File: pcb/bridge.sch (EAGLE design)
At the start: 46 parts, among them IC1 MEGA8-AI, IC4 78L05SMD, IC5 LM358D, Q1 16MHz, X1 PN61729-S

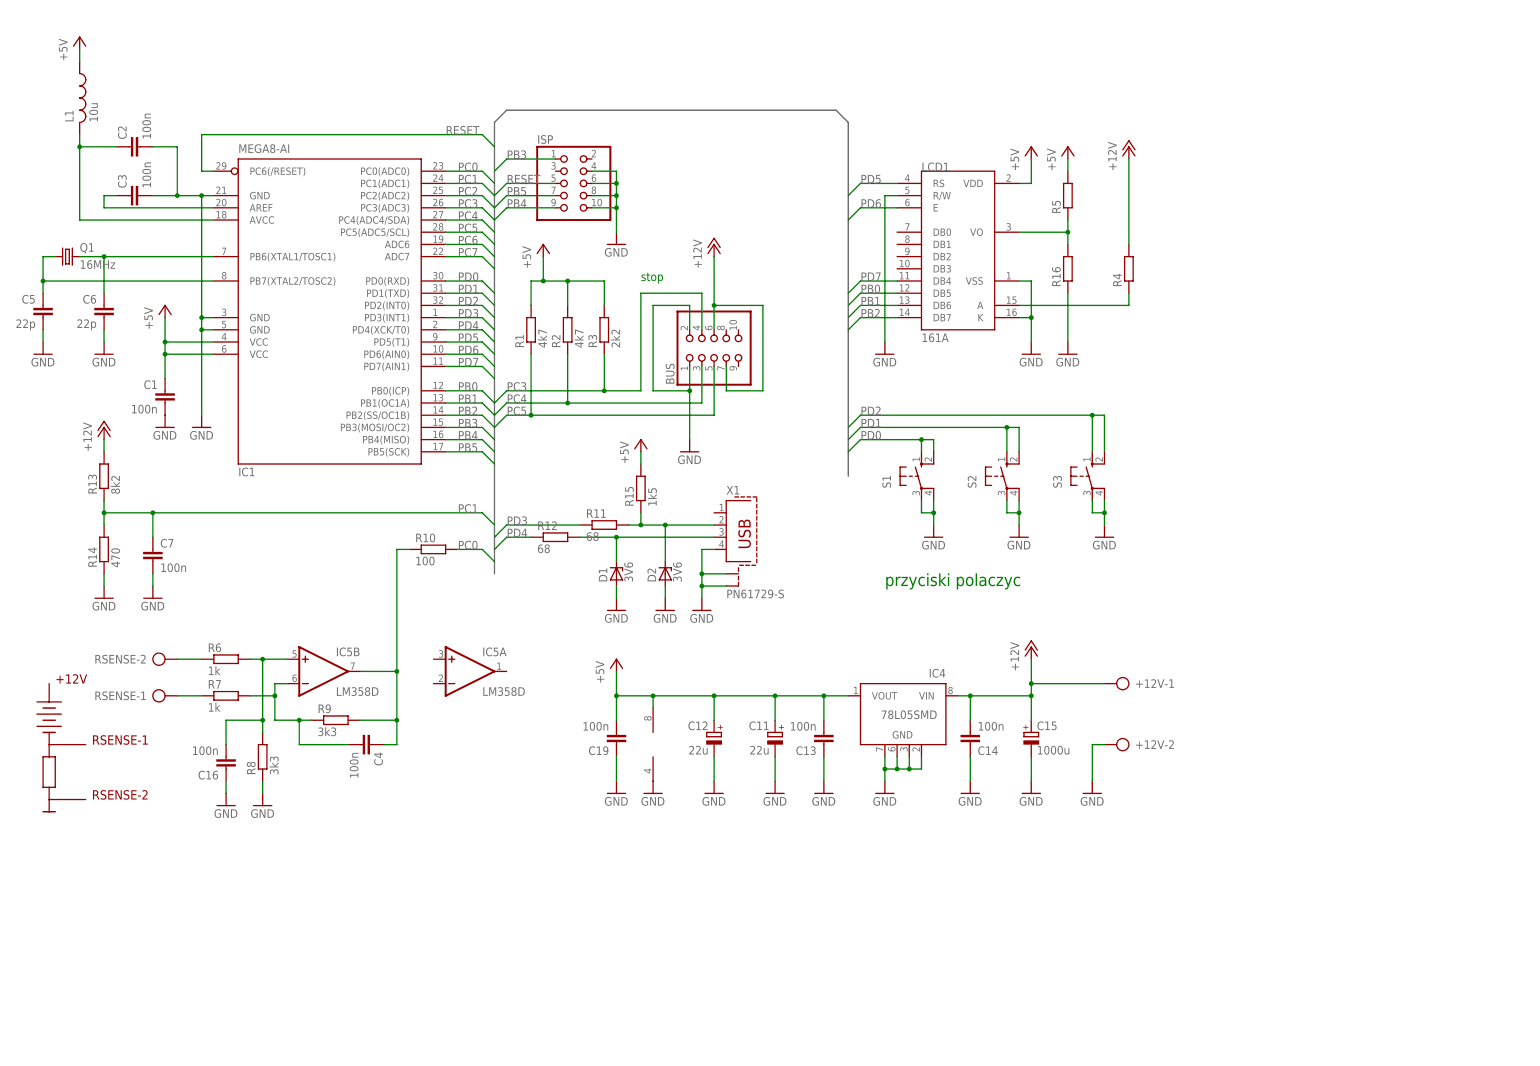
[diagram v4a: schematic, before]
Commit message: Changed op-amp resistors values on the bridge schematic and general clean-up.
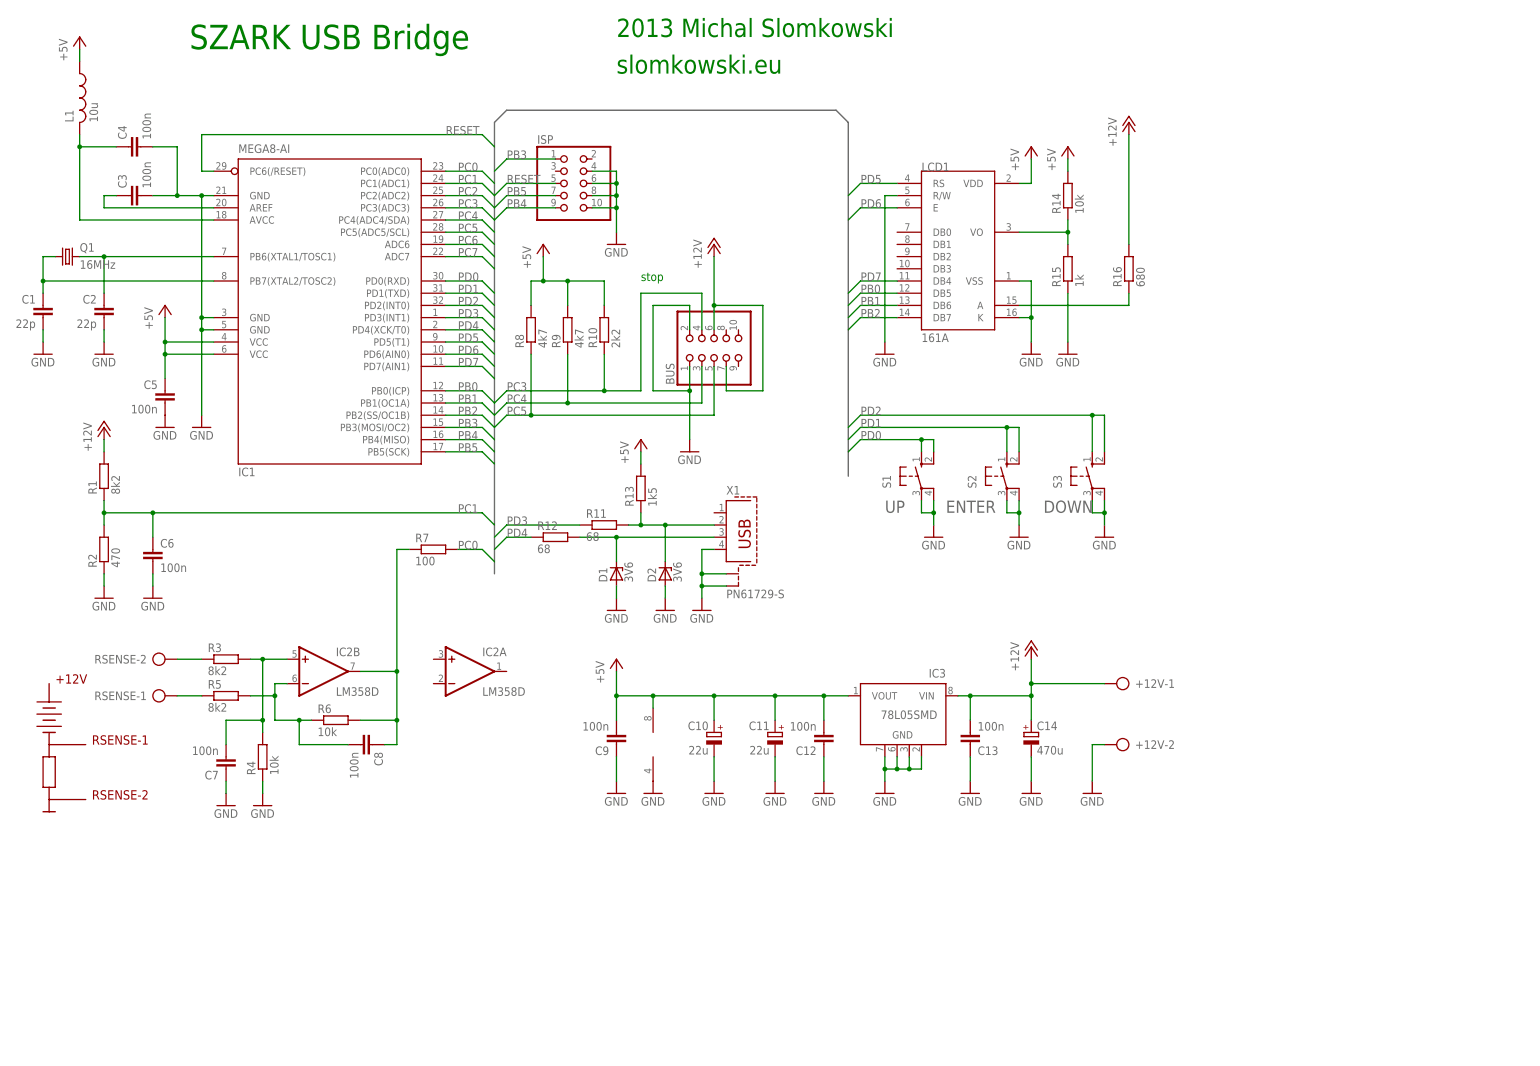
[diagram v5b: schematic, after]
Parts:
- removed C15: 1000u, rcl:CPOL-EUE5-10.5
- removed C16: 100n, rcl:C-EUC1210
- added C10: 22u, rcl:CPOL-EUE2,5-6E
- added C8: 100n, rcl:C-EUC1206
- C1, C2: value 100n -> 22p
- C12: value 22u -> 100n; device rcl:CPOL-EUE2,5-6E -> rcl:C-EUC1210
- C14: value 100n -> 470u; device rcl:C-EUC1210 -> rcl:CPOL-EUE5-10.5
- C5, C6: value 22p -> 100n
- C7: device rcl:C-EUC1206 -> rcl:C-EUC1210
- R1: value 4k7 -> 8k2
- R10: value 100 -> 2k2
- R13: value 8k2 -> 1k5
- R14: value 470 -> 10k
- R15: value 1k5 -> 1k
- R16: value (none) -> 680; device rcl:R-EU_M1206 -> rcl:R-EU_0207/12
- R2: value 4k7 -> 470
- R3: value 2k2 -> 8k2
- R4: value (none) -> 10k; device rcl:R-EU_0207/12 -> rcl:R-EU_M1206
- R5: value (none) -> 8k2
- R6: value 1k -> 10k
- R7: value 1k -> 100
- R8, R9: value 3k3 -> 4k7
- renumbered C19 to C9, IC4 to IC3, IC5 to IC2
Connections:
- net +12V: now also C13.2, C14.+, R1.2, R16.2; no longer C14.2, C15.+, R13.2, R4.2
- net +5V: now also C10.+, C12.2, C5.1, R10.2, R13.2, R14.2, R8.2, R9.2; no longer C1.1, C12.+, C13.2, R1.2, R15.2, R2.2, R3.2, R5.2
- net GND: now also C10.-, C12.1, C14.-, C4.2, C7.1, R15.1, R2.1, R4.1; no longer C12.-, C14.1, C15.-, C16.1, C7.2, R14.1, R16.1, R8.1
- net N$1: now also C7.2, R3.2, R4.2; no longer C16.2, R6.2, R8.2
- net N$10: now also C4.1; no longer C2.1
- net N$11: now also C1.1; no longer C5.1
- net N$2: now also R16.1; no longer R4.1
- net N$21: now also R5.1; no longer R7.1
- net N$29: now also R3.1; no longer R6.1
- net N$3: now also R14.1, R15.2; no longer R16.2, R5.1
- net N$4: now also C8.2, R5.2, R6.1; no longer C4.2, R7.2, R9.1
- net N$5: now also R13.1; no longer R15.1
- net N$9: now also C2.1; no longer C6.1
- net NET3: now also C8.1, R6.2, R7.1; no longer C4.1, R10.1, R9.2
- net PC0: now also R7.2; no longer R10.2
- net PC1: now also C6.1, R1.1, R2.2; no longer C7.1, R13.1, R14.2
- net PC3: now also R10.1; no longer R3.1
- net PC4: now also R9.1; no longer R2.1
- net PC5: now also R8.1; no longer R1.1
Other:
- note added: "2013 Michal Slomkowski"
- note added: "DOWN"
- note added: "ENTER"
- note added: "SZARK USB Bridge"
- note added: "UP"
- note added: "slomkowski.eu"
- note removed: "przyciski polaczyc"
- moved on the sheet: C1, C13, C2, C4, C5, C6, C7, R1, R10, R13, R14, R15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
